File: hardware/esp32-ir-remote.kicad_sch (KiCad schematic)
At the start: 60 parts, among them J1 ESP32-WROOM-32E-Breakout, J2 USB_C_Receptacle_USB2.0_14P, Q1 Q_NPN_BCE, Q2 Q_NPN_BCE, Q3 IRLML6344, SW1 RESET, SW2 BOOT, U1 AP63203WU, U2 CH340C, U3 ESP32-WROOM-32E, U4 TSOP382xx, U5 AM2302

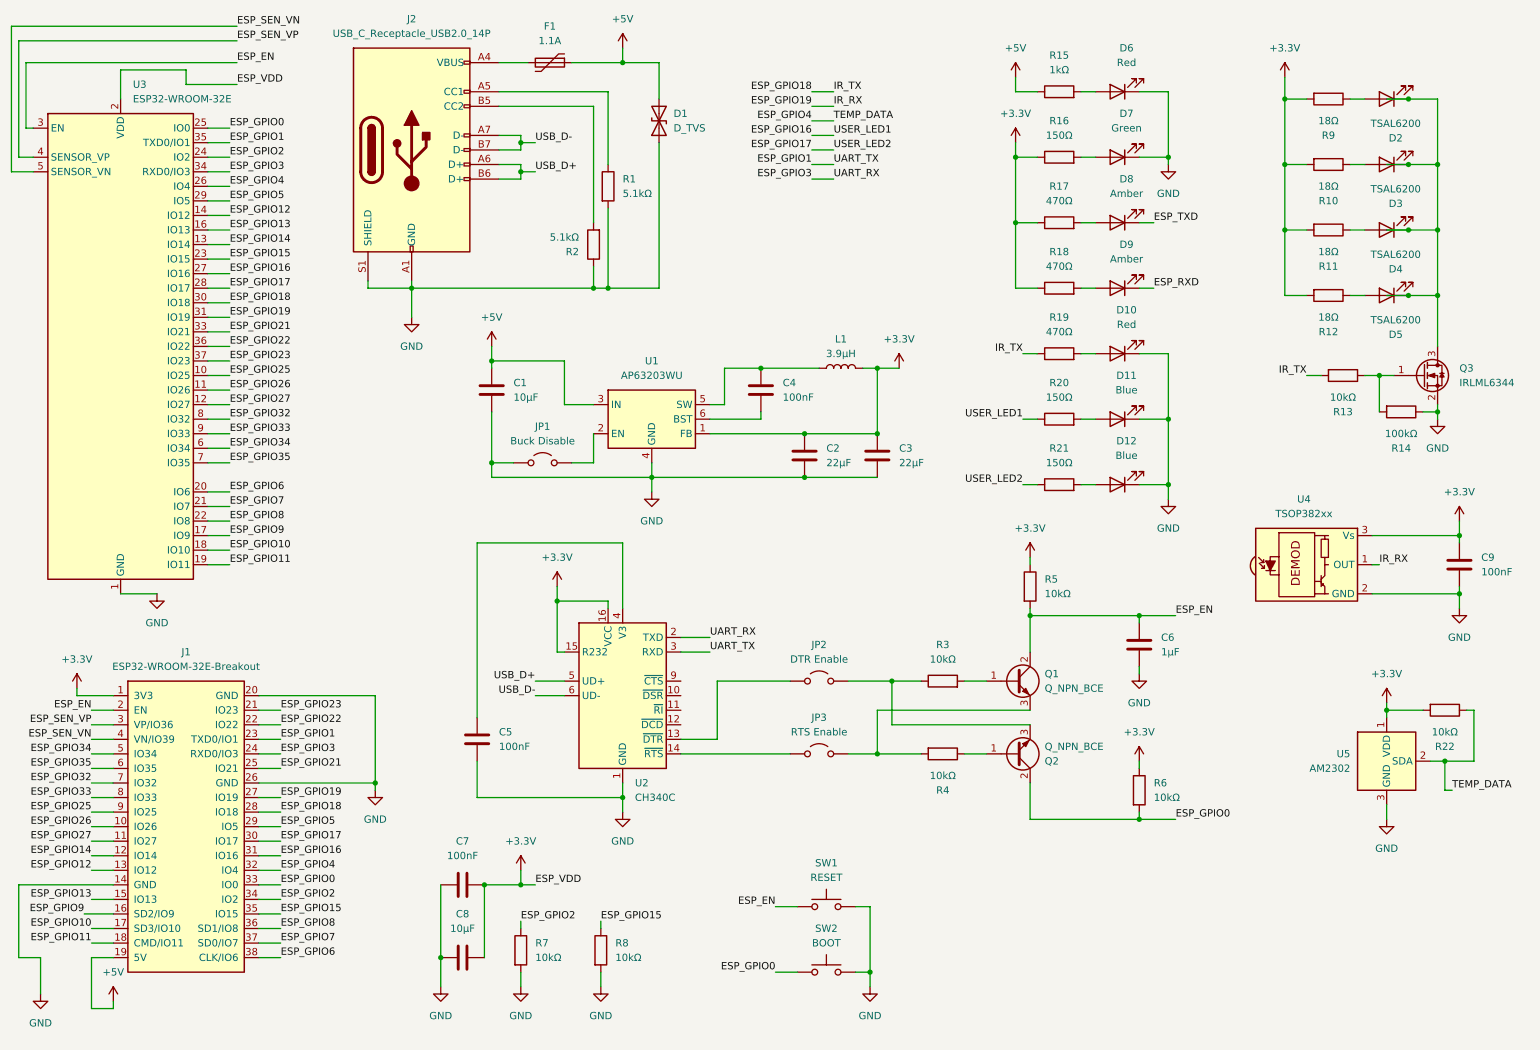
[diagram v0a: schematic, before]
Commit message: Add footprints, blue LED MOSFET drivers, and JLCPCB part assignments
Schematic updates:
- Add Q4, Q5 (2N7002) as low-side MOSFET drivers for blue LEDs
- Add R23, R24 (100kΩ) gate pulldown resistors
- Add R25 (1kΩ) as second blue LED current limiting resistor
- Assign footprints to all components for PCB layout
- Add LCSC part numbers for JLCPCB assembly
- Add PWR_FLAG symbols for ERC compliance
- Add no-connect flags on unused CH340C pins

Library additions:
- Add SRP5030T-4R7M inductor footprint and symbol from SnapEDA

Note: CH340C VCC still needs to be rewired from +3.3V to +5V

🤖 Generated with [Claude Code](https://claude.com/claude-code)

Co-Authored-By: Claude Opus 4.5 <noreply@anthropic.com>
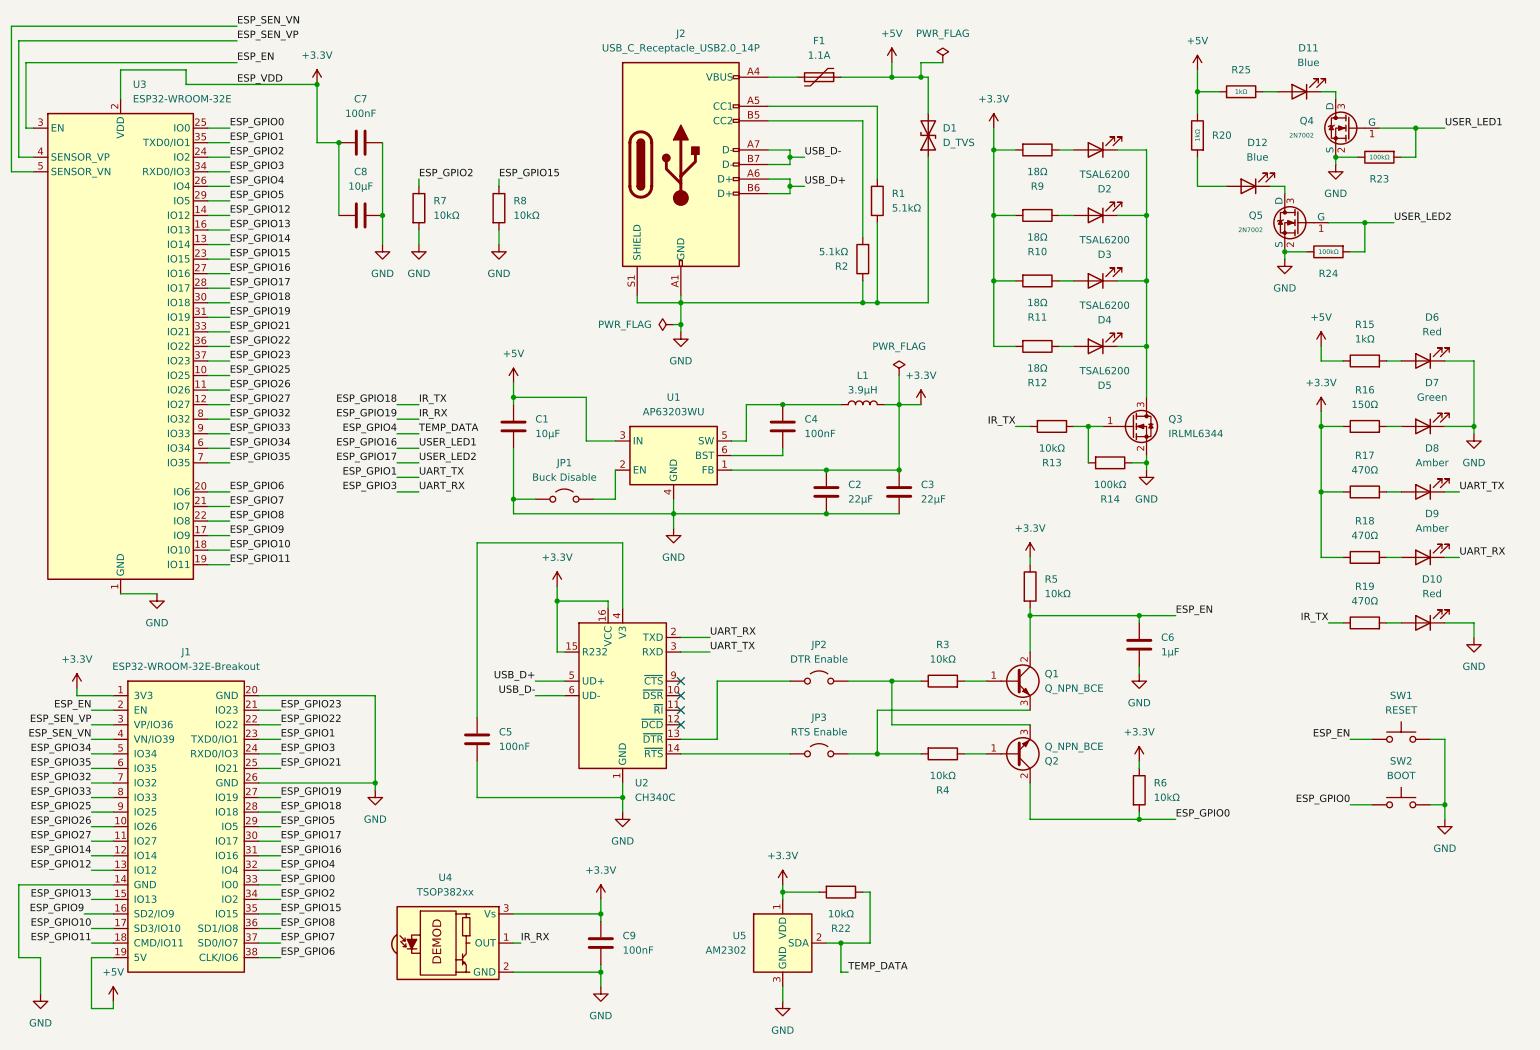
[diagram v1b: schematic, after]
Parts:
- removed R20, R21: 150Ω, symbol Device:R
- added Q4, Q5: 2N7002, PCM_JLCPCB:Q_SOT-23, symbol PCM_JLCPCB-Transistors:NMOS,2N7002
- added R20, R25: 1kΩ, PCM_JLCPCB:R_0805, symbol PCM_JLCPCB-Resistors:0805,1kΩ
- added R23, R24: 100kΩ, PCM_JLCPCB:R_0603, symbol PCM_JLCPCB-Resistors:0603,100kΩ
- C1, C2, C3, C6, C8: footprint (none) -> Capacitor_SMD:C_0805_2012Metric
- C4, C5, C7, C9: footprint (none) -> Capacitor_SMD:C_0603_1608Metric
- D1: footprint (none) -> Diode_SMD:D_SMB
- D10, D11, D12, D6, D7, D8, D9: footprint (none) -> LED_THT:LED_D3.0mm
- D2, D3, D4, D5: footprint (none) -> LED_THT:LED_D5.0mm
- F1: footprint (none) -> Fuse:Fuse_1812_4532Metric
- J2: footprint (none) -> Connector_USB:USB_C_Receptacle_GCT_USB4085
- JP2, JP3: footprint (none) -> Connector_PinHeader_2.54mm:PinHeader_1x02_P2.54mm_Vertical
- L1: footprint (none) -> lib:INDM5752X300N
- Q1, Q2, Q3: footprint (none) -> Package_TO_SOT_SMD:SOT-23
- R1, R10, R11, R12, R13, R14, R15, R16, R17, R18, R19, R2, R22, R3, R4, R5, R6, R7, R8, R9: footprint (none) -> Resistor_SMD:R_1206_3216Metric
- SW1, SW2: footprint (none) -> Button_Switch_THT:SW_PUSH_6mm
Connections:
- net ESP_RXD is gone; now on net ESP_GPIO3: D9.1 (K)
- net ESP_TXD is gone; now on net ESP_GPIO1: D8.1 (K)
- net +5V: now also R20.2, R25.1
- net ESP_GPIO16: now also Q4.1 (G), R23.1
- net ESP_GPIO17: now also Q5.1 (G), R24.1
- net GND: now also Q4.2 (S), Q5.2 (S), R23.2, R24.2; no longer D11.1 (K), D12.1 (K)
- net at D12.2 (A): now also R20.1
- net at D11.2 (A): now also R25.2
- new net: D12.1 (K), Q5.3 (D)
- new net: D11.1 (K), Q4.3 (D)
- no-connect marks 0 -> 4
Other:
- moved on the sheet: C1, C2, C3, C4, C7, C8, C9, D1, D10, D11, D12, D2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

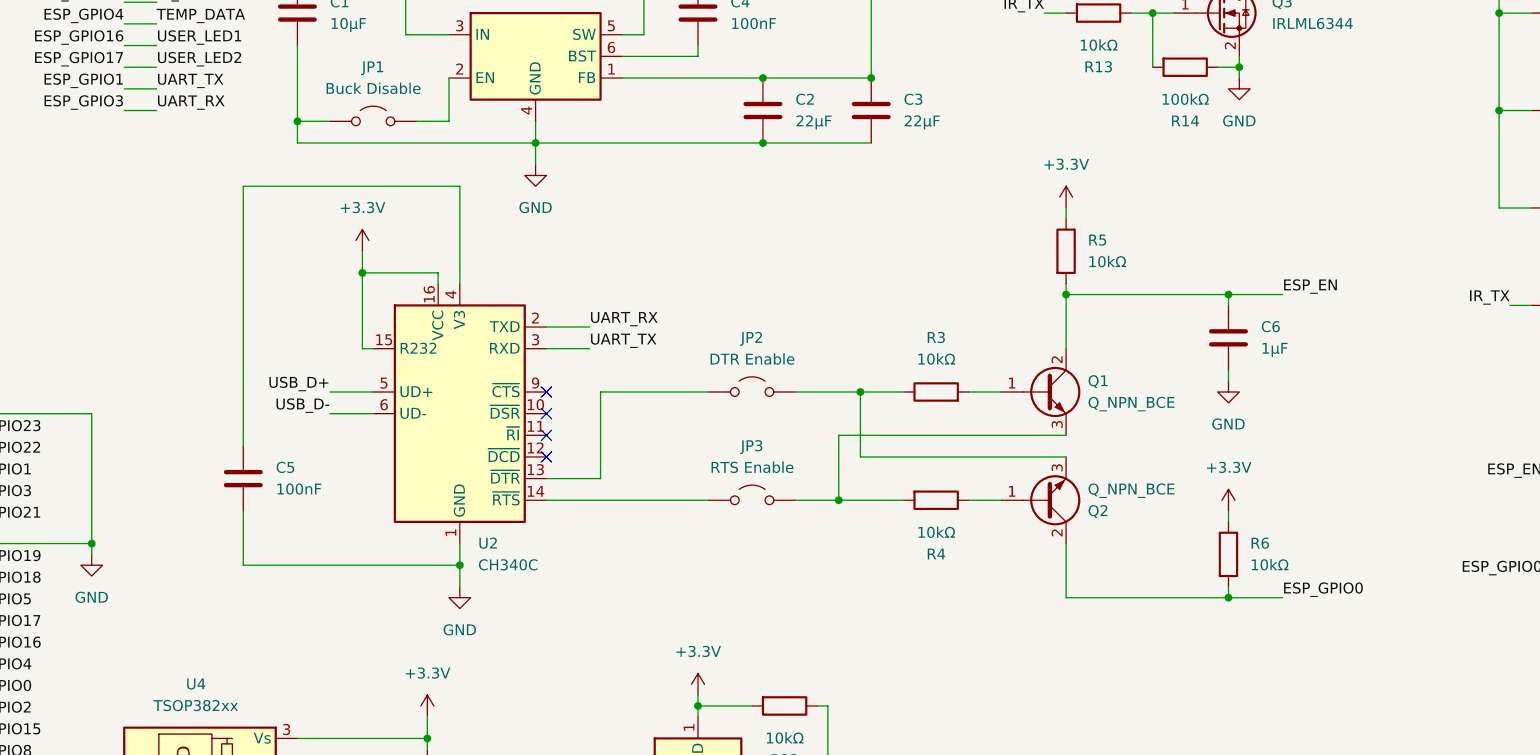
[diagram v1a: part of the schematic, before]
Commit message: Add circuit.md format and document ESP32 IR Remote schematic
Introduces a new markdown-based circuit description format that captures
both topology and design rationale. The format supports:
- Net and component declarations with bracket syntax
- Inline passives: [VCC --- 10kΩ --- EN]
- Design properties: [dropout ==> 1.2V]
- Subcircuit references: @./power-supply.circuit.md

Circuit documentation for ESP32 IR Remote board:
- power-supply.circuit.md: USB-C, protection, AP63203 buck
- usb-serial.circuit.md: CH340C with auto-reset circuit
- esp32-mcu.circuit.md: ESP32-WROOM-32E module
- ir-transmitter.circuit.md: 4x TSAL6200 with MOSFET driver
- ir-receiver.circuit.md: TSOP38238 for development
- temp-sensor.circuit.md: DHT22/AM2302
- status-leds.circuit.md: Serial and user indicators

Also includes:
- Parser and KiCad export scripts
- Component datasheets
- Updated schematic and PCB layout
- BOM export

🤖 Generated with [Claude Code](https://claude.com/claude-code)

Co-Authored-By: Claude Opus 4.5 <noreply@anthropic.com>
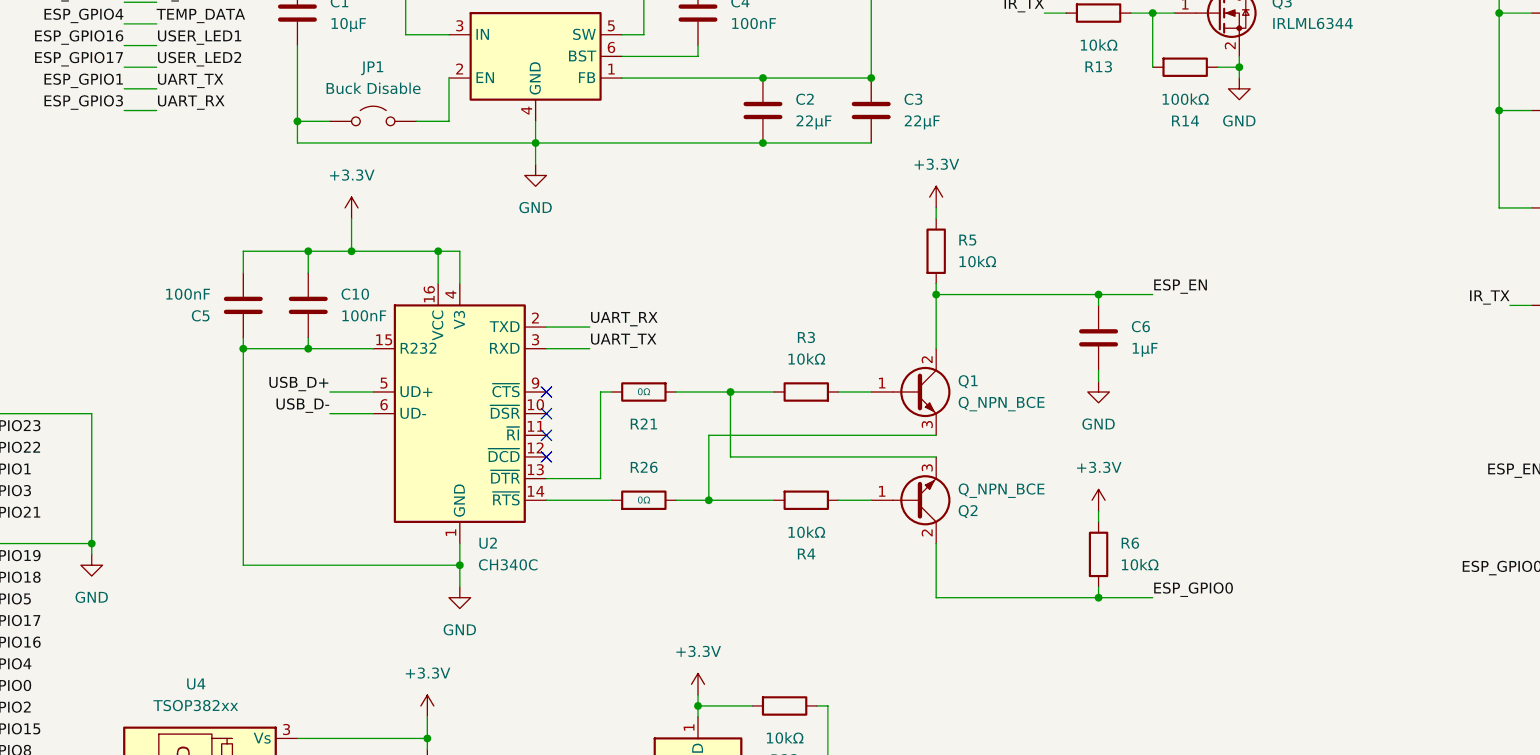
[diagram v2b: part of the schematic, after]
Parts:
- removed JP2: DTR Enable, Connector_PinHeader_2.54mm:PinHeader_1x02_P2.54mm_Vertical, symbol Jumper:Jumper_2_Open
- removed JP3: RTS Enable, Connector_PinHeader_2.54mm:PinHeader_1x02_P2.54mm_Vertical, symbol Jumper:Jumper_2_Open
- added C10: 100nF, Capacitor_SMD:C_0603_1608Metric, symbol Device:C
- added R21, R26: 0Ω, PCM_JLCPCB:R_0603, symbol PCM_JLCPCB-Resistors:0603,0Ω
- C1, C8: LCSC (none) -> C15850
- C2, C3: LCSC (none) -> C45783
- C4, C5, C7, C9: LCSC (none) -> C14663
- C6: LCSC (none) -> C28323
- D2, D3: LCSC (none) -> C55528
- J1: LCSC (none) -> C2685155
- J2: LCSC (none) -> C7095263
- JP1: LCSC (none) -> C124375
- L1: footprint lib:INDM5752X300N -> lib:IND-SMD_L6.7-W6.7
- Q1, Q2: LCSC (none) -> C2146
- Q3: LCSC (none) -> C8545
- R1, R2: LCSC (none) -> C27834
- R10, R11, R12, R13, R22, R9: LCSC (none) -> C17955
- R14: LCSC (none) -> C149504
- R15: LCSC (none) -> C17513
- R16: LCSC (none) -> C17471
- R17, R18, R19: LCSC (none) -> C17710
- R3, R4, R5, R6, R7, R8: LCSC (none) -> C17414
- U1: LCSC (none) -> C780769
- U2: LCSC (none) -> C84681
- U3: LCSC (none) -> C701341
- U4: LCSC (none) -> C141632
- U5: LCSC (none) -> C83988
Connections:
- net +3.3V: now also C5.2, U2.4 (V3), C10.1; no longer U2.15 (R232)
- net GND: now also C5.1, U2.15 (R232), C10.2; no longer C5.2
- net at Q2.3 (E), R3.1: now also R21.1
- net at Q1.3 (E), R4.2: now also R26.2
- net at U2.14 (~{RTS}): now also R26.1
- net at U2.13 (~{DTR}): now also R21.2
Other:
- moved on the sheet: C5, C6, Q1, Q2, R3, R4, R5, R6
